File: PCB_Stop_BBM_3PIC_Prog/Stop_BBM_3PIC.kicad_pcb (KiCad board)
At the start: 2 copper layers, 46 x 62 mm, 11 parts, among them J1 Haut parleur (MOUSE), J2 Conn_01x05_Male, J3 Conn_01x06, J4 Conn_01x01_Male, J5 Conn_01x01_Male, J6 Conn_01x01_Male

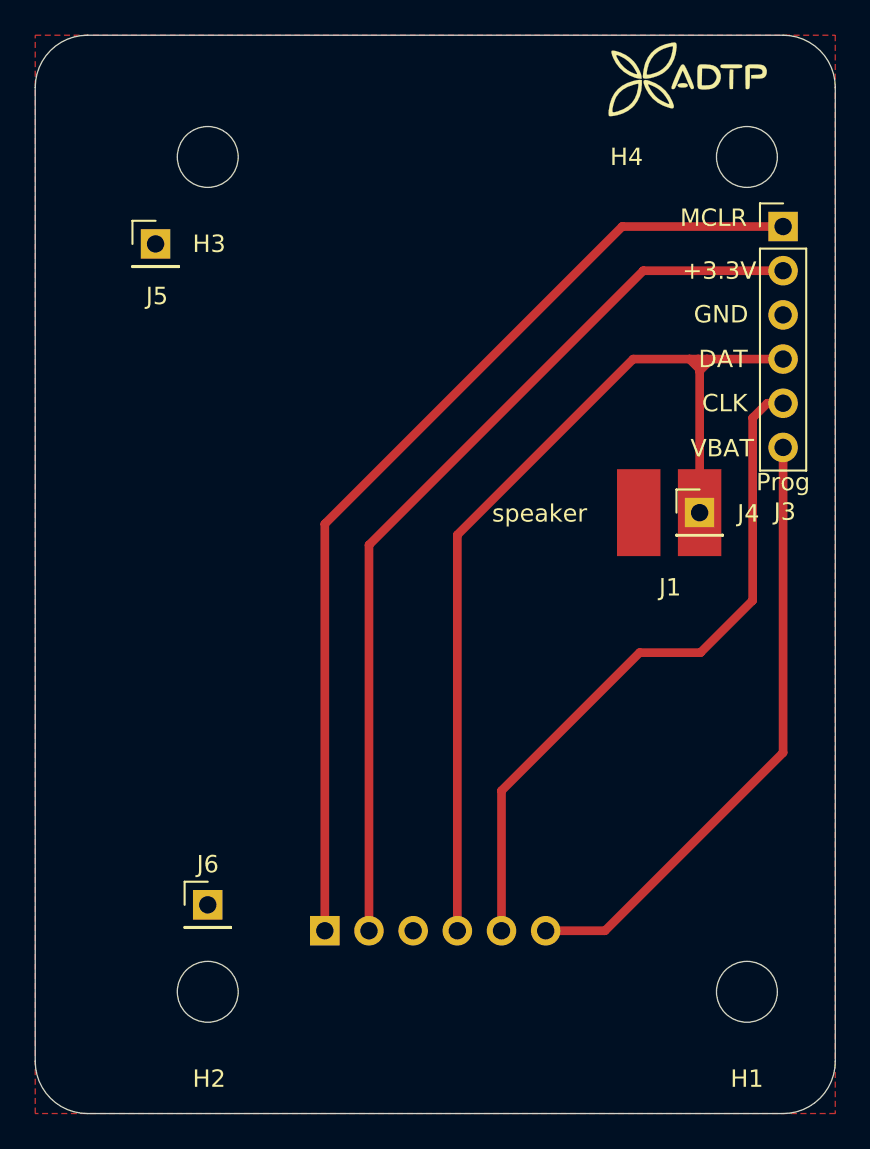
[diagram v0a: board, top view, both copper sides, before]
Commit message: Ajout MCLR et VBAT sur F.CU + Gerber en 3 fichiers
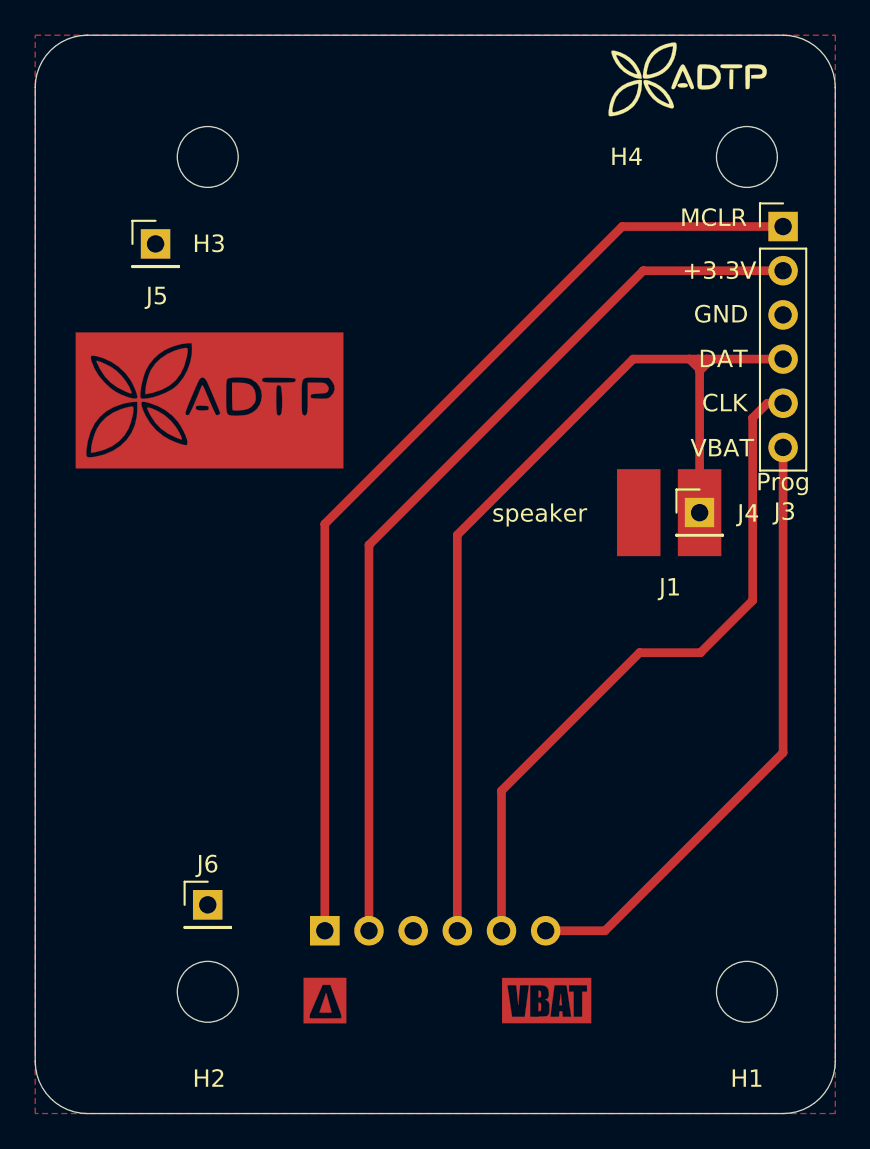
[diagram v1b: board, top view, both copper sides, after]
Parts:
- added G***: LOGO, prog:delta-top, F.Cu at (95.7, 163.5)
- added G***: LOGO, prog:VBAT-top, F.Cu at (108.4, 163.5)
- added G***: LOGO, prog:logo_ADTP_neg_v2_top, F.Cu at (89.0, 129.0)

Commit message: Modifié pour EUROCIRCUIT  + Devis
discuter de la sérigraphie
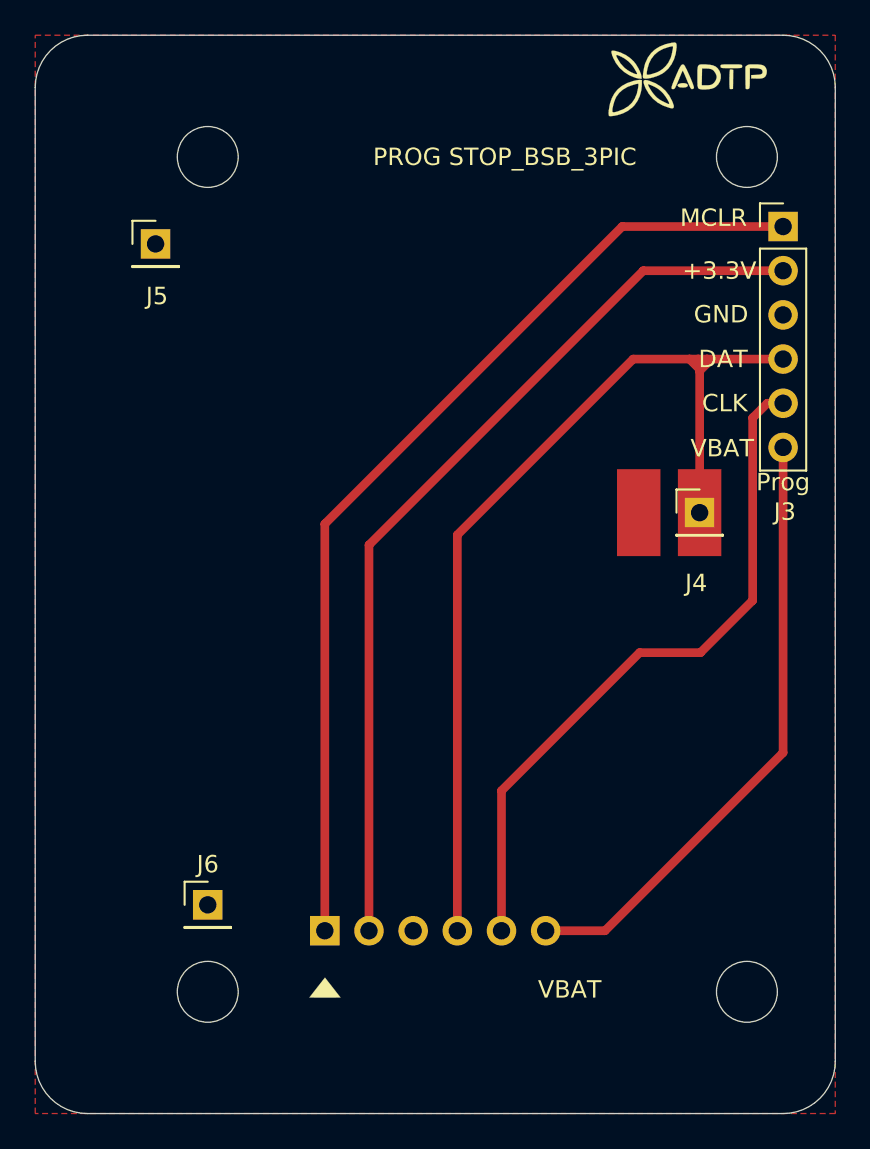
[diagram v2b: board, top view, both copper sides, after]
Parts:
- removed the G*** at (95.7, 163.5)
- removed the G*** at (108.4, 163.5)
- removed the G*** at (89.0, 129.0)
- added G***: LOGO, prog:Triangle_Fskils, F.Cu at (95.6, 162.8)
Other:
- board text added: "PROG STOP_BSB_3PIC"
- board text removed: "speaker"

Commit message: PRODUCTION: Démo semaine prochaine
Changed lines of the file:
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@@
-(kicad_pcb (version 20171130) (host pcbnew "(5.1.4)-1")
+(kicad_pcb (version 20171130) (host pcbnew "(5.1.10)-1")
   (general
     (thickness 1.6)
@@
     (mod_text_width 0.15)
     (pad_size 1.7 1.7)
-    (pad_drill 1)
+    (pad_drill 0.8)
     (pad_to_mask_clearance 0)
     (aux_axis_origin 82 167)
@@
       (effects (font (size 1 1) (thickness 0.15)))
     )
-    (pad 6 thru_hole oval (at 0 12.7) (size 1.7 1.7) (drill 1) (layers *.Cu *.Mask)
+    (pad 6 thru_hole oval (at 0 12.7) (size 1.7 1.7) (drill 0.8) (layers *.Cu *.Mask)
       (net 1 Vbatt))
-    (pad 5 thru_hole oval (at 0 10.16) (size 1.7 1.7) (drill 1) (layers *.Cu *.Mask)
+    (pad 5 thru_hole oval (at 0 10.16) (size 1.7 1.7) (drill 0.8) (layers *.Cu *.Mask)
       (net 7 ISCPCLK))
-    (pad 4 thru_hole oval (at 0 7.62) (size 1.7 1.7) (drill 1) (layers *.Cu *.Mask)
+    (pad 4 thru_hole oval (at 0 7.62) (size 1.7 1.7) (drill 0.8) (layers *.Cu *.Mask)
       (net 5 ISCPDAT))
-    (pad 3 thru_hole oval (at 0 5.08) (size 1.7 1.7) (drill 1) (layers *.Cu *.Mask)
+    (pad 3 thru_hole oval (at 0 5.08) (size 1.7 1.7) (drill 0.8) (layers *.Cu *.Mask)
       (net 2 GND))
-    (pad 2 thru_hole oval (at 0 2.54) (size 1.7 1.7) (drill 1) (layers *.Cu *.Mask)
+    (pad 2 thru_hole oval (at 0 2.54) (size 1.7 1.7) (drill 0.8) (layers *.Cu *.Mask)
       (net 3 +3V3_5V))
-    (pad 1 thru_hole rect (at 0 0) (size 1.7 1.7) (drill 1) (layers *.Cu *.Mask)
+    (pad 1 thru_hole rect (at 0 0) (size 1.7 1.7) (drill 0.8) (layers *.Cu *.Mask)
       (net 4 MCLR))
   )
@@
       (effects (font (size 1 1) (thickness 0.15)))
     )
-    (pad 1 thru_hole rect (at 0 0) (size 1.7 1.7) (drill 1) (layers *.Cu *.Mask)
+    (pad 1 thru_hole rect (at 0 0) (size 1.7 1.7) (drill 0.8) (layers *.Cu *.Mask)
       (net 8 "Net-(J5-Pad1)"))
   )
@@
       (effects (font (size 1 1) (thickness 0.15)))
     )
-    (pad 1 thru_hole rect (at 0 0) (size 1.7 1.7) (drill 1) (layers *.Cu *.Mask)
+    (pad 1 thru_hole rect (at 0 0) (size 1.7 1.7) (drill 0.8) (layers *.Cu *.Mask)
       (net 9 "Net-(J6-Pad1)"))
   )
